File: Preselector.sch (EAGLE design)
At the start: 134 parts, among them IC58 LMZ31707RVQ, Q2 FDV303N, X1 0733660061, X2 0733660061, X3 0733660061, X4 0733660061, X5 0733660061, X6 0733660061, X7 0733660061, X8 0733660061

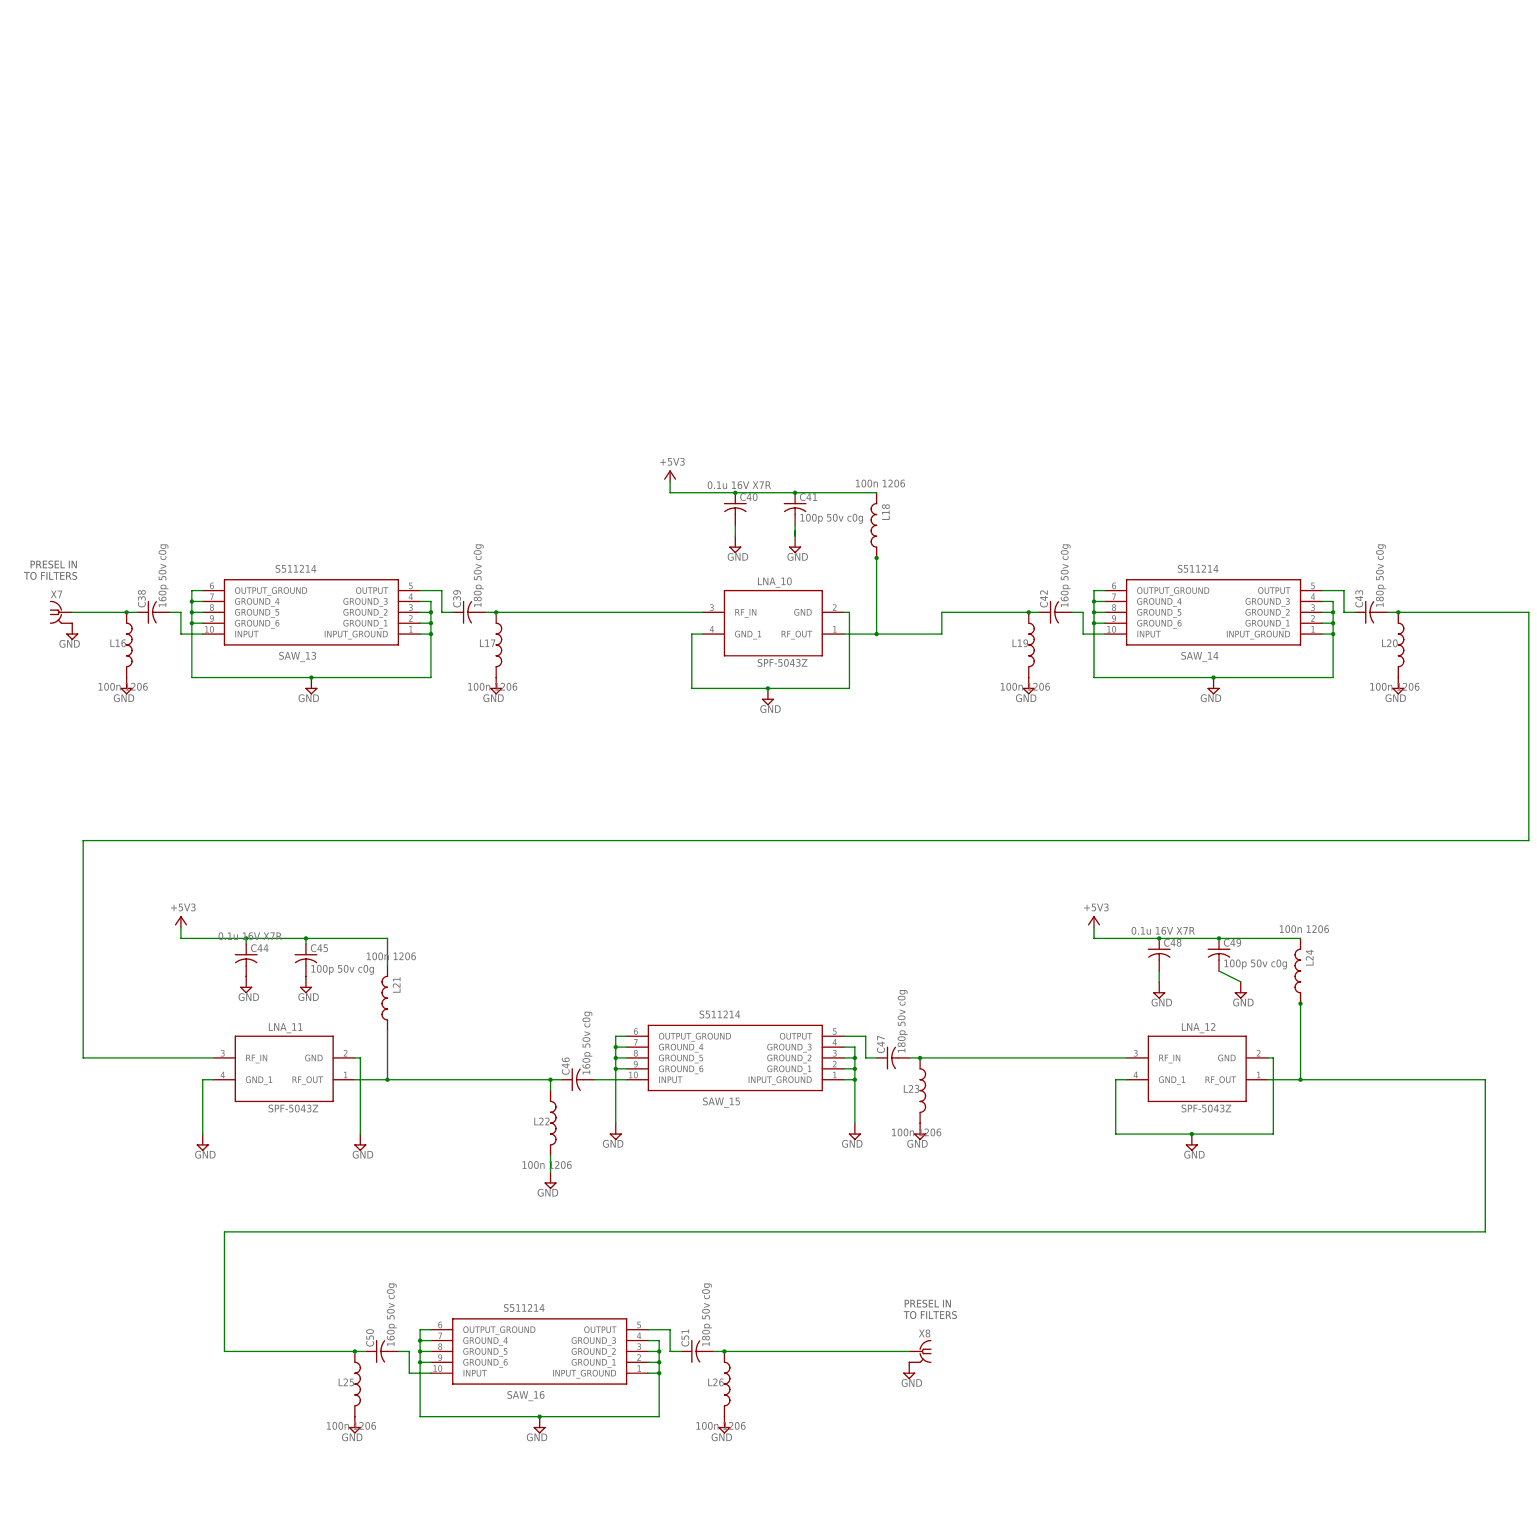
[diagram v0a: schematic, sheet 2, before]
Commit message: Added connectors on 4m band and also copied LDO over
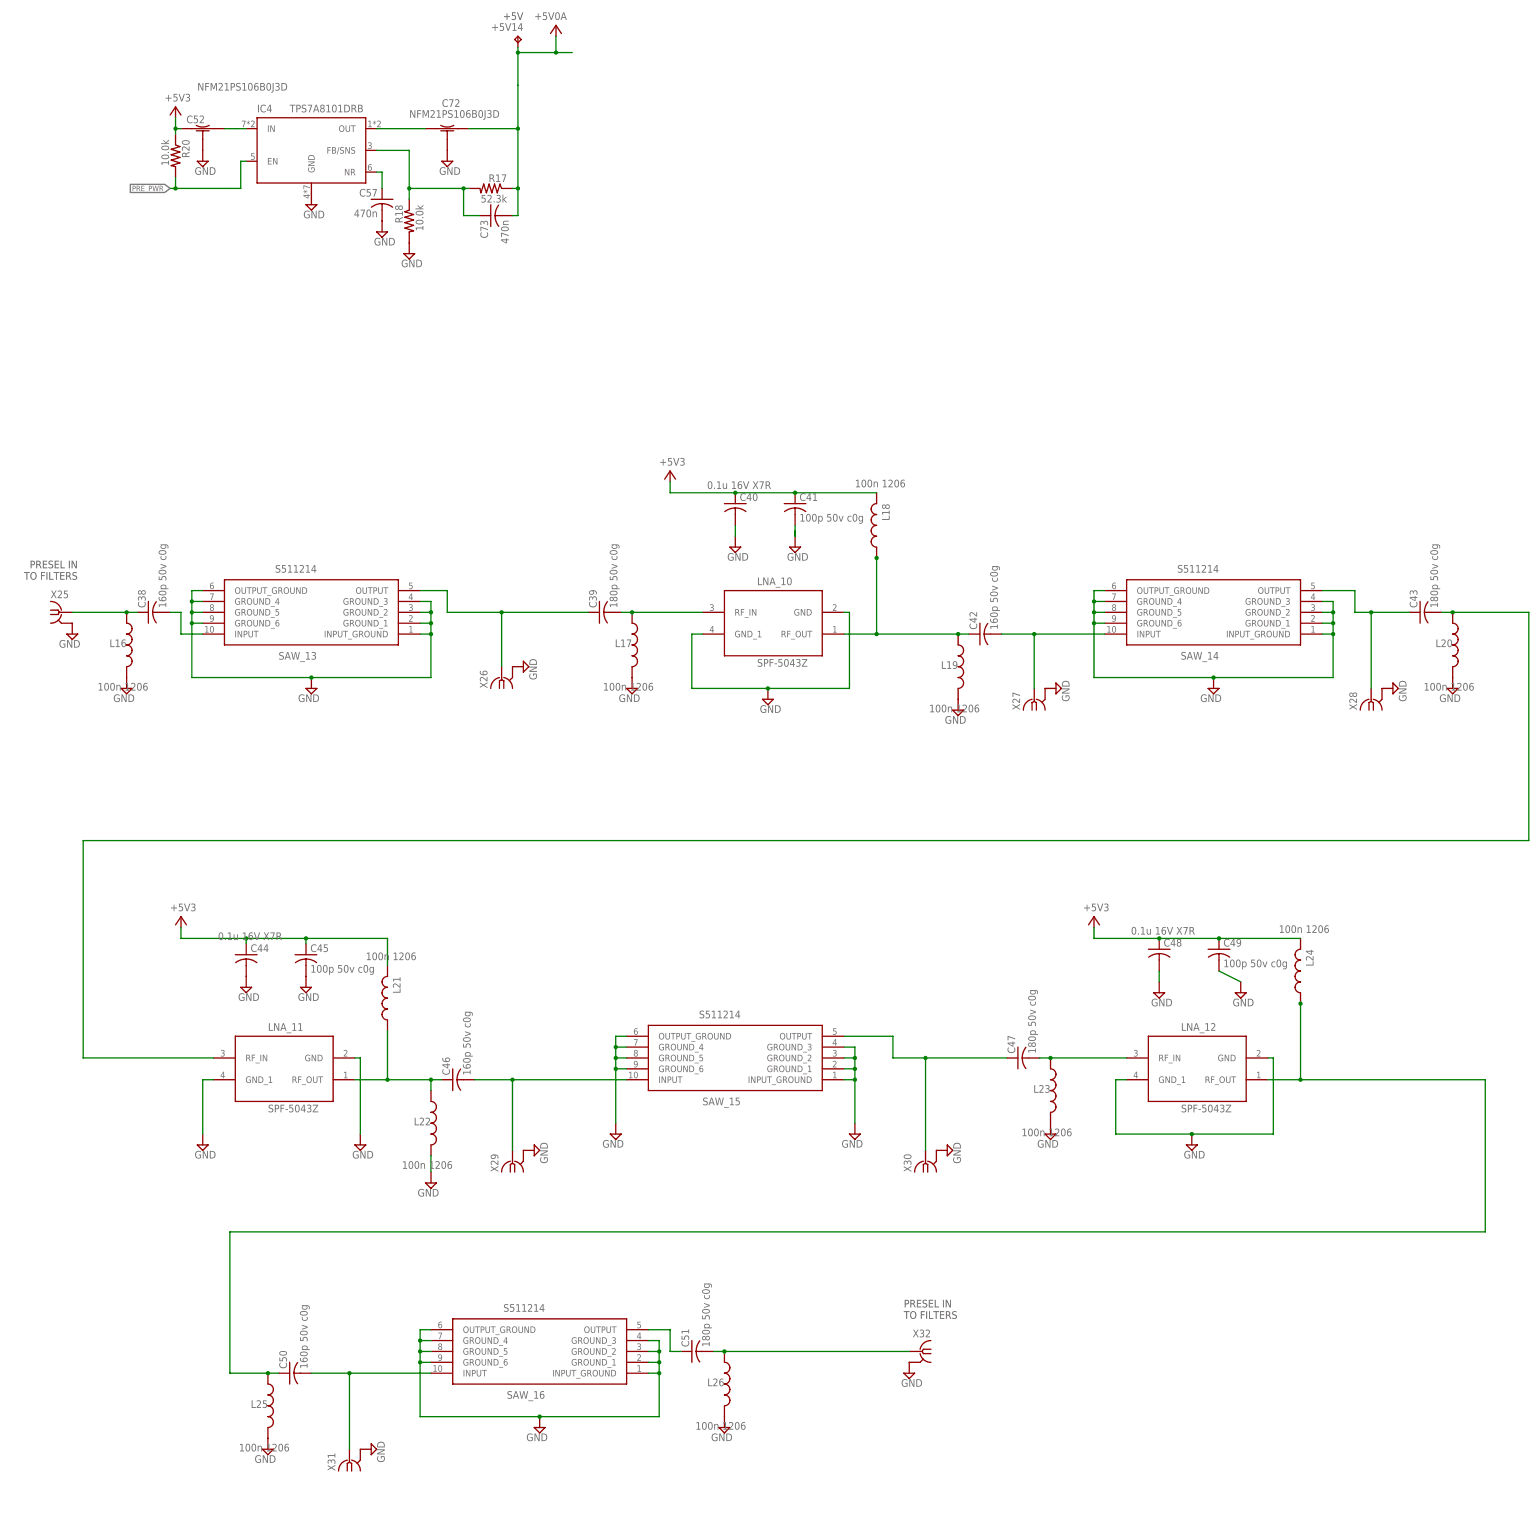
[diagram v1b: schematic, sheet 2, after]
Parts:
- added +5V14: TPTP20SQ, testpad:TPTP20SQ
- added C52, C72: NFM21PS106B0J3D, DEEP EDDY:NFM21PS
- added C57, C73: 470n, rcl:C-USC0402K
- added IC4: TPS7A8101DRB, DEEP EDDY:TPS7A8101DRB
- added R17: 52.3k, rcl:R-US_R0603
- added R18, R20: 10.0k, rcl:R-US_R0603
- added X26, X27, X28, X29, X30, X31: 0733660061, con-coax:BU-SMA-V
- renumbered X7 to X25, X8 to X32
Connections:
- new net +5V0A: +5V14.TP, C72.OUT, C73.2, R17.1
- new net N$2: C73.1, IC4.FB/SNS, R17.2, R18.1
- new net N$3: C57.1, IC4.NR
- new net N$4: C52.OUT, IC4.IN
- new net N$6: C72.IN, IC4.OUT
- new net PRE_PWR: IC4.EN, R20.2
- net +5V3: now also C52.IN, R20.1
- net GND: now also C52.GND, C57.2, C72.GND, IC4.GND, R18.2, X26G$1.GND, X27G$1.GND, X28G$1.GND, X29G$1.GND, X30G$1.GND, X31G$1.GND
- net SAW_13_OUT: now also X26G$1.1
- net SAW_14_IN: now also X27G$1.1
- net SAW_14_OUT: now also X28G$1.1
- net SAW_15_IN: now also X29G$1.1
- net SAW_15_OUT: now also X30G$1.1
- net SAW_16_IN: now also X31G$1.1
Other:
- note added: "+5V"
- note added: "ENABLE PRE_PWR FOR BITE1"
- note added: "REV B HAD PCHAN FET HERE GROUND GATE"
- moved on the sheet: C39, C42, C43, C46, C47, C50, L17, L19, L20, L22, L23, L25

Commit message: Connected the connectors (schematic). Ripped up traces from board.
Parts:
- added X10, X11, X12, X13, X14, X15, X16, X17, X18, X19, X20, X21, X22, X23, X24, X7, X8, X9: 0733660061, con-coax:BU-SMA-V
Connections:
- net 2M_RF_IN_2 renamed 2M_RF_IN17
- net 2M_RF_IN_5 renamed N$9
- net LNA_3_IN renamed 2M_RF_IN20
- removed net 1.25M_RF_IN_: C21.2, SAW_6.INPUT
- removed net 1.25M_RF_IN_1: C25.2, SAW_7.INPUT
- removed net 1.2M5_RF_IN4: C22.1, SAW_6.OUTPUT
- removed net 2M_RF_IN_3: C4.2, L2.2, SAW_2.INPUT
- removed net 2M_RF_IN_6: C8.1, L4.1, LNA_2.RF_OUT
- removed net LNA_3_OUT: C9.2, LNA_3.RF_IN
- removed net N$14: SAW_7.OUTPUT, SAW_8.INPUT
- removed net N$15: C29.2, SAW_9.INPUT
- removed net N$16: C30.1, SAW_9.OUTPUT
- removed net N$17: C33.2, SAW_10.INPUT
- removed net N$18: C34.1, SAW_10.OUTPUT
- removed net N$19: C37.2, SAW_11.INPUT
- removed net N$20: SAW_11.OUTPUT, SAW_12.INPUT
- removed net N$56: SAW_12.OUTPUT, X6G$1.1
- new net 2M_RF_IN1: C29.2, SAW_9.INPUT, X18G$1.1
- new net 2M_RF_IN10: C34.1, SAW_10.OUTPUT, X21G$1.1
- new net 2M_RF_IN11: SAW_11.OUTPUT, SAW_12.INPUT, X23G$1.1
- new net 2M_RF_IN12: C17.2, SAW_5.INPUT, X10G$1.1
- new net 2M_RF_IN13: C21.2, SAW_6.INPUT, X12G$1.1
- new net 2M_RF_IN14: C22.1, SAW_6.OUTPUT, X13G$1.1
- new net 2M_RF_IN15: C25.2, SAW_7.INPUT, X14G$1.1
- new net 2M_RF_IN16: SAW_7.OUTPUT, SAW_8.INPUT, X15G$1.1
- new net 2M_RF_IN19: C8.2, L4.1, LNA_2.RF_OUT
- new net 2M_RF_IN5: C33.2, SAW_10.INPUT, X20G$1.1
- new net 2M_RF_IN7: C37.2, SAW_11.INPUT, X22G$1.1
- new net 2M_RF_IN9: C30.1, SAW_9.OUTPUT, X19G$1.1
- new net N$11: C9.1, L6.2, SAW_3.OUTPUT, X6G$1.1
- new net N$7: SAW_12.OUTPUT, X24G$1.1
- net 1.25M_RF_IN: no longer C17.2, SAW_5.INPUT
- net 1.25M_RF_IN3: now also X11G$1.1
- net 2M_RF_IN: now also X8G$1.1; no longer X2G$1.1
- net 2M_RF_IN2: now also X9G$1.1; no longer X3G$1.1
- net 2M_RF_IN3: now also X16G$1.1; no longer X4G$1.1
- net 2M_RF_IN4: now also X17G$1.1; no longer X5G$1.1
- net 2M_RF_IN_4: now also X4G$1.1
- net 2M_RF_IN_7: now also C8.1, X5G$1.1; no longer C8.2
- net 2M_RF_IN_9: now also C9.2, LNA_3.RF_IN; no longer C9.1, L6.2, SAW_3.OUTPUT
- net GND: now also C4.2, L2.2, X10G$1.GND, X11G$1.GND, X12G$1.GND, X13G$1.GND, X14G$1.GND, X15G$1.GND, X16G$1.GND, X17G$1.GND, X18G$1.GND, X19G$1.GND, X20G$1.GND, X21G$1.GND, X22G$1.GND, X23G$1.GND, X24G$1.GND, X3G$1.1, X7G$1.GND, X8G$1.GND, X9G$1.GND
- net SAW_1_OUT: now also X2G$1.1
- net SAW_4_OUT: now also X7G$1.1; no longer C12.2
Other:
- moved on the sheet: C12, C4, C5, C8, C9, X2

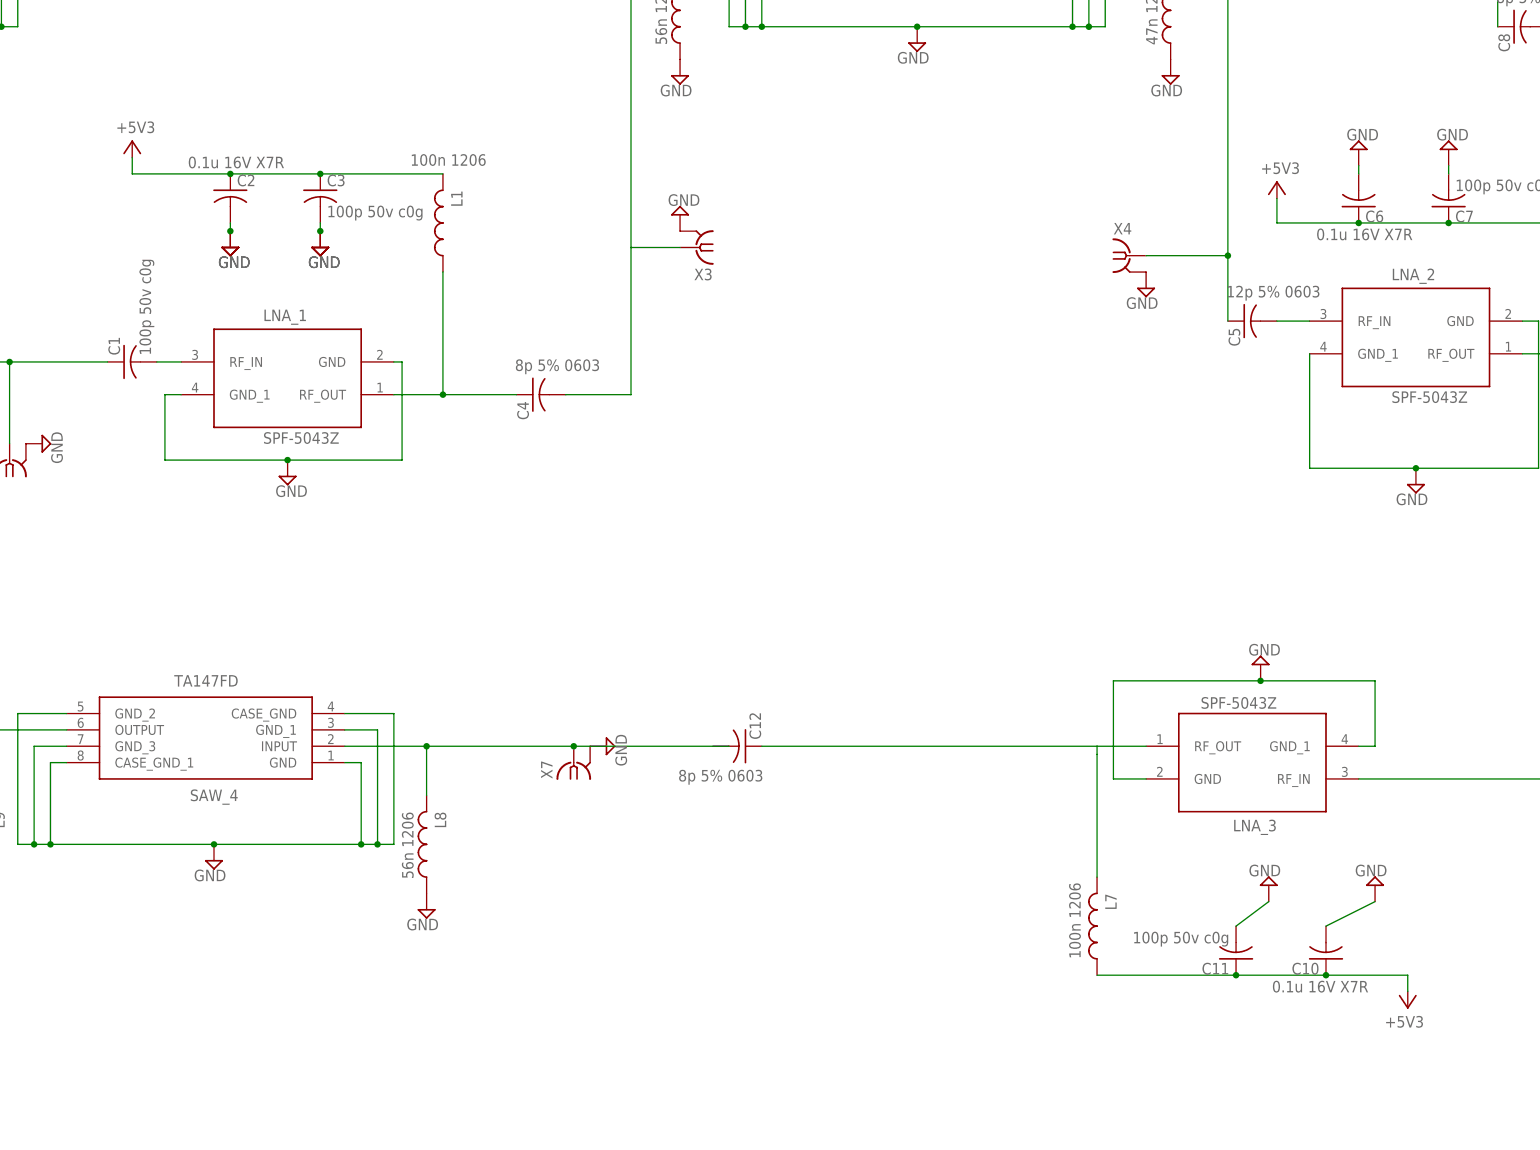
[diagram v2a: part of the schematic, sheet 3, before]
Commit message: started fixing some of the ERC errors in the schematic. DRC is for the board. Cut down on half of the errors and approved a few that were from the POWER SYSTEM page.
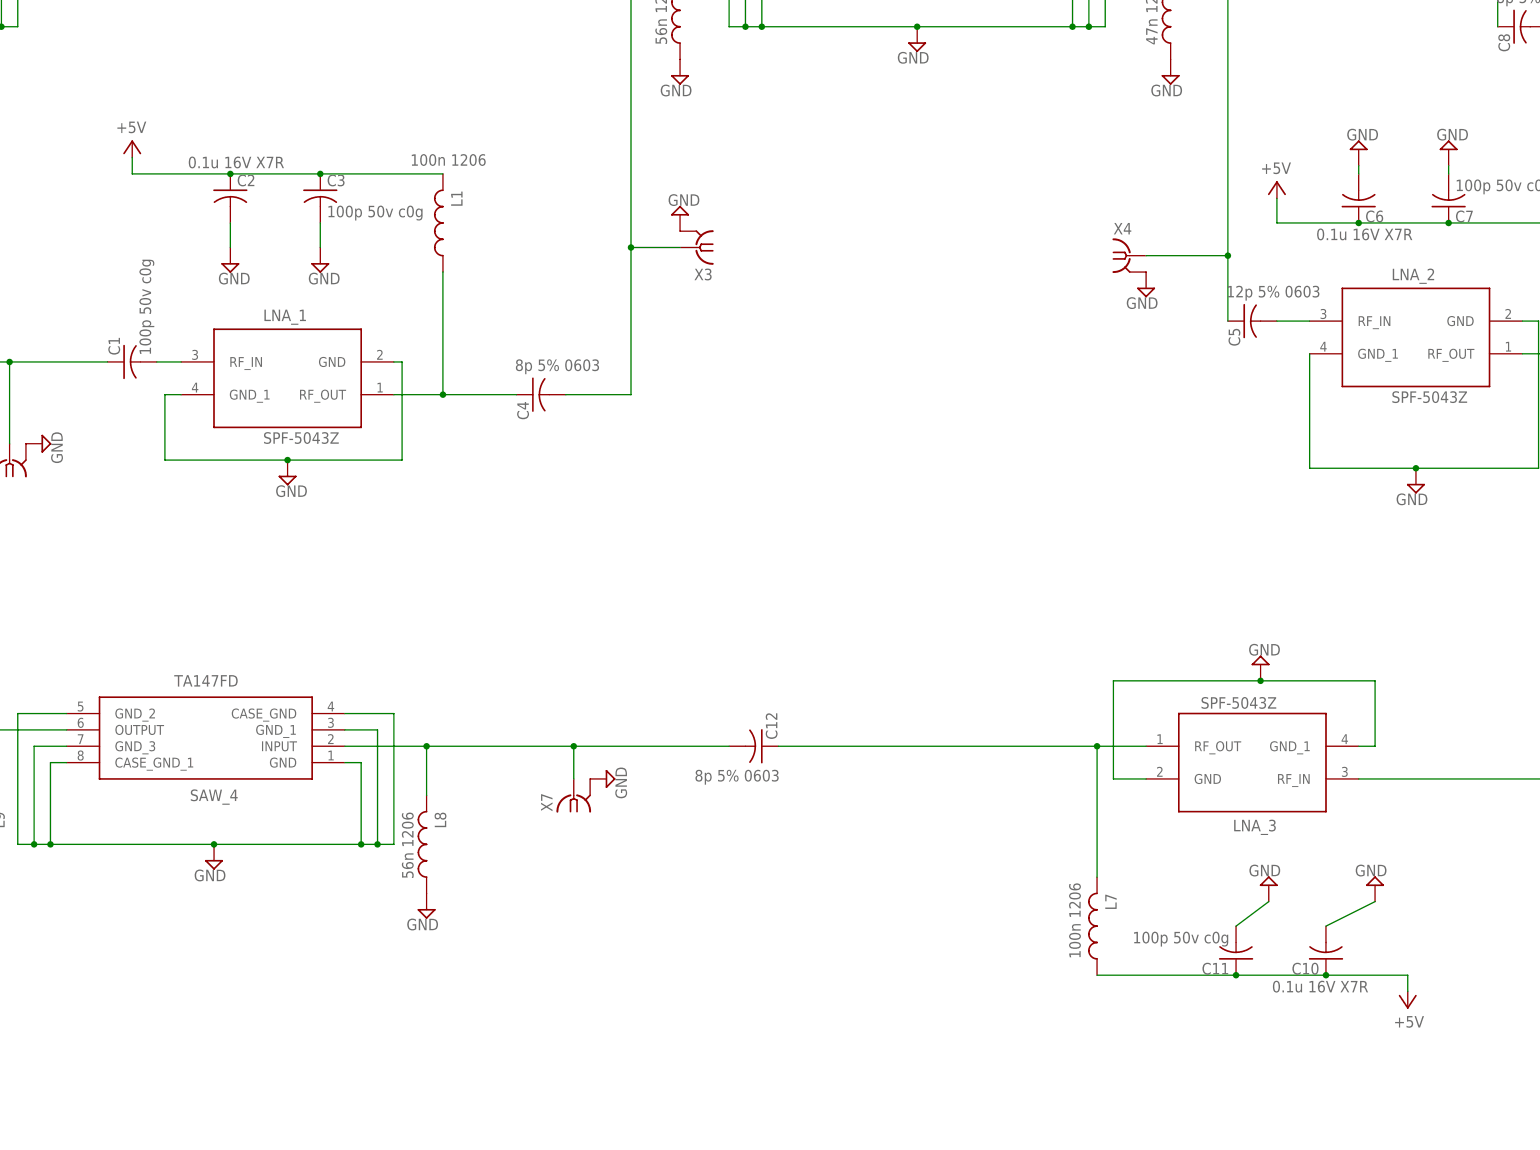
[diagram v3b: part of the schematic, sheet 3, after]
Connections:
- net 2M_RF_IN12 renamed SAW_5_IN
- net 2M_RF_IN13 renamed LNA_5_OUT
- new net LNA_4_OUT: C17.1, L10.1, LNA_4.RF_OUT
- new net SAW_5_OUT: C18.1, SAW_5.OUTPUT, X11G$1.1
- net +5V: now also C10.1, C11.1, C15.1, C16.1, C19.1, C2.1, C20.1, C23.1, C24.1, C27.1, C28.1, C3.1, C31.1, C32.1, C35.1, C36.1, C48.1, C49.1, C6.1, C7.1, L1.2, L10.2, L11.2, L12.1, L13.2, L14.2, L15.2, L24.2, L4.2, L7.1
- net +5V3: no longer C10.1, C11.1, C15.1, C16.1, C19.1, C2.1, C20.1, C23.1, C24.1, C27.1, C28.1, C3.1, C31.1, C32.1, C35.1, C36.1, C48.1, C49.1, C6.1, C7.1, L1.2, L10.2, L11.2, L13.2, L14.2, L15.2, L24.2, L4.2, L7.1
- net 1.25M_RF_IN: now also C14.1, X9G$1.1; no longer C17.1, L10.1, LNA_4.RF_OUT
- net 1.25M_RF_IN3: no longer C18.1, SAW_5.OUTPUT, X11G$1.1
- net 2M_RF_IN2: no longer C14.1, X9G$1.1
- net SAW_4_OUT: now also C12.2
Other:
- moved on the sheet: C12, L12, X7
